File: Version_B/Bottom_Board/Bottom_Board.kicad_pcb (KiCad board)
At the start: 2 copper layers, 74.8 x 84.5 mm, 52 parts, among them J1 Conn_02x03_Top_Bottom, J2 Conn_02x03_Top_Bottom, J3 Conn_01x02_Pin, J5 DIN-5, J6 Conn_01x02_Pin, J7 Conn_01x02_Pin, J8 Screw_Terminal_01x04, J9 Screw_Terminal_01x04, SW2 SW_DIP_x04, U1 LM324, U2 LM324

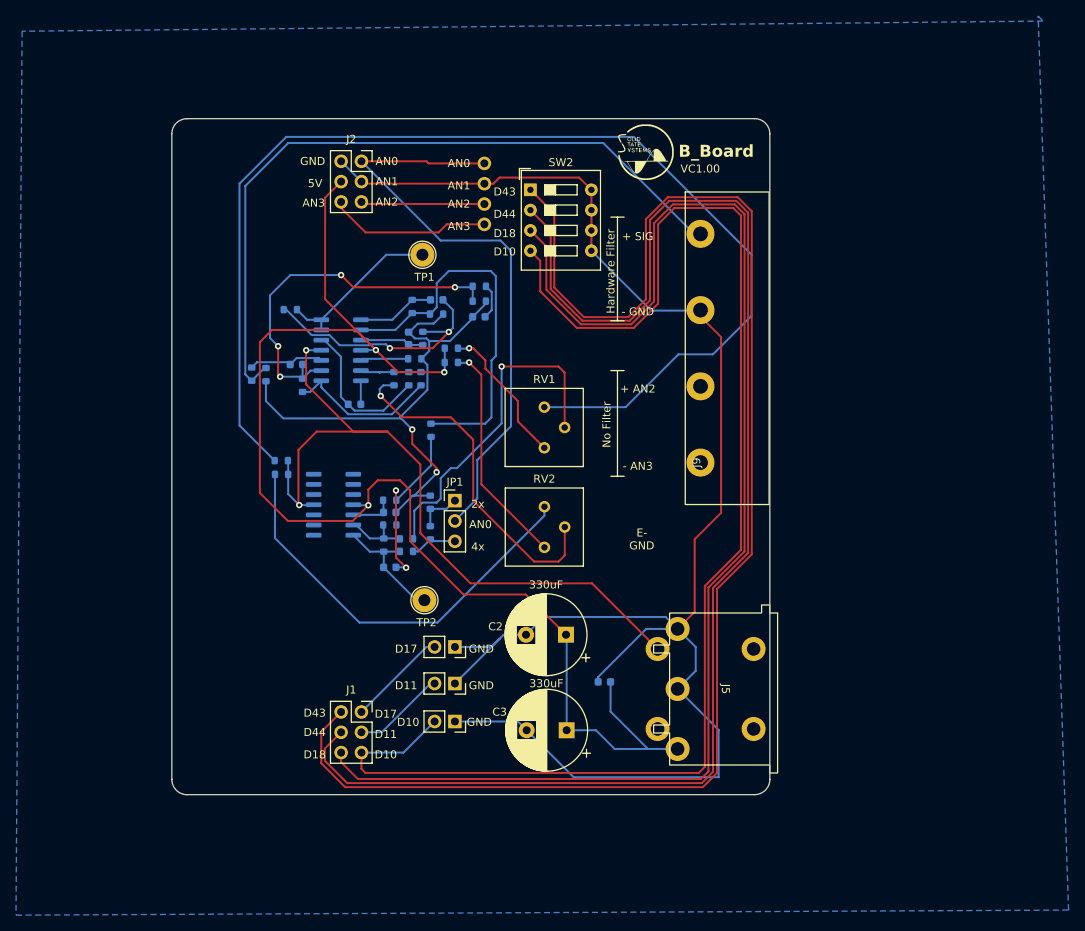
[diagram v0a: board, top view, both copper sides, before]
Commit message: soft pcb changes: 90 degree term block, din connector scooted in, connected grounds
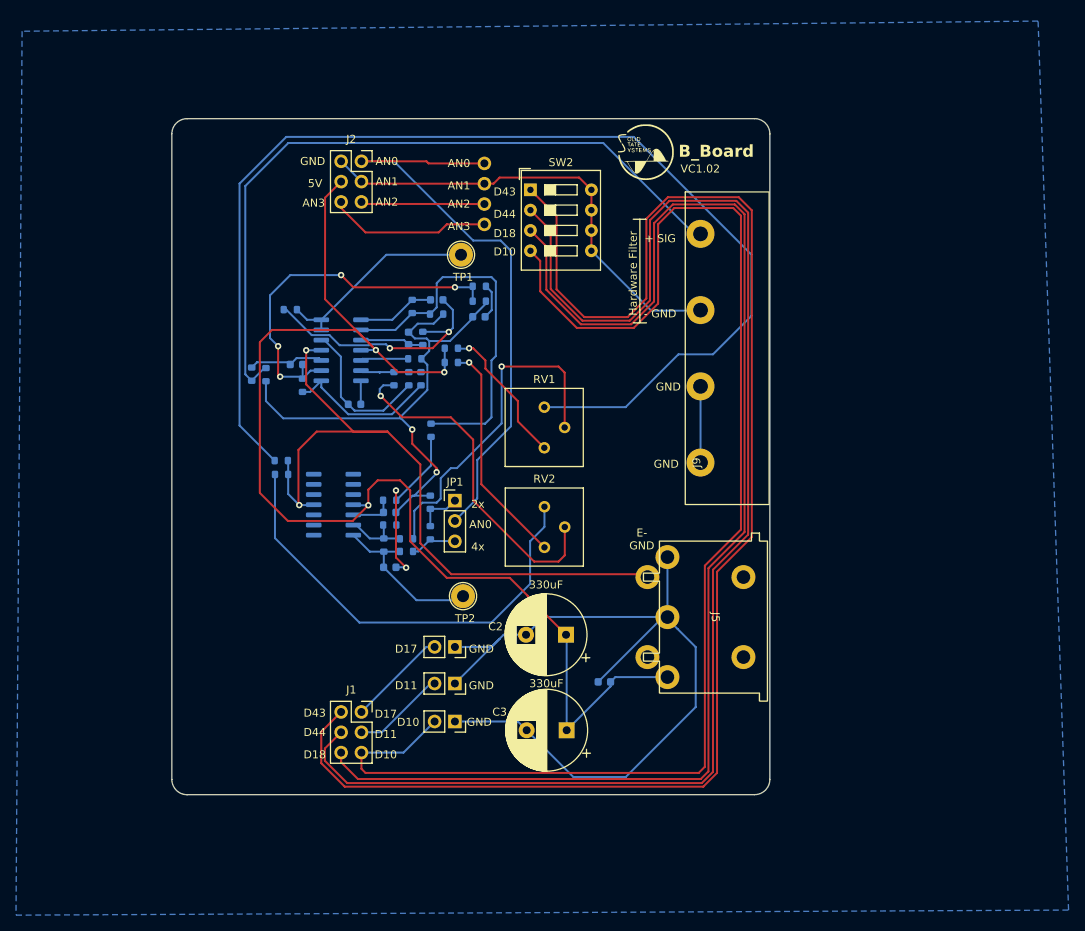
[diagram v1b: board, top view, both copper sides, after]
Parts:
- moved J5 9.07 mm to (167.9, 125.3)
- moved TP2 4.85 mm to (136.4, 122.7)
- moved TP1 4.83 mm to (136.1, 80.0)
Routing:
- net AN1: track 279.0 -> 240.5 mm
- net 5V: track 167.8 -> 158.4 mm
- net Net-(U1D--): track 20.8 -> 25.7 mm
- net Net-(C4-Pad1): track 15.5 -> 20.0 mm
- net -5V: track 95.9 -> 91.6 mm
- net Net-(R18-Pad1): track 52.7 -> 56.6 mm
- net Net-(U1A--): track 47.8 -> 46.8 mm
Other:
- board text added: "VC1.02"
- board text removed: "+ AN2"
- board text removed: "- AN3"
- board text removed: "No Filter"
- board text removed: "VC1.00"

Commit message: ads1015 on bottom board and aesthetic changes
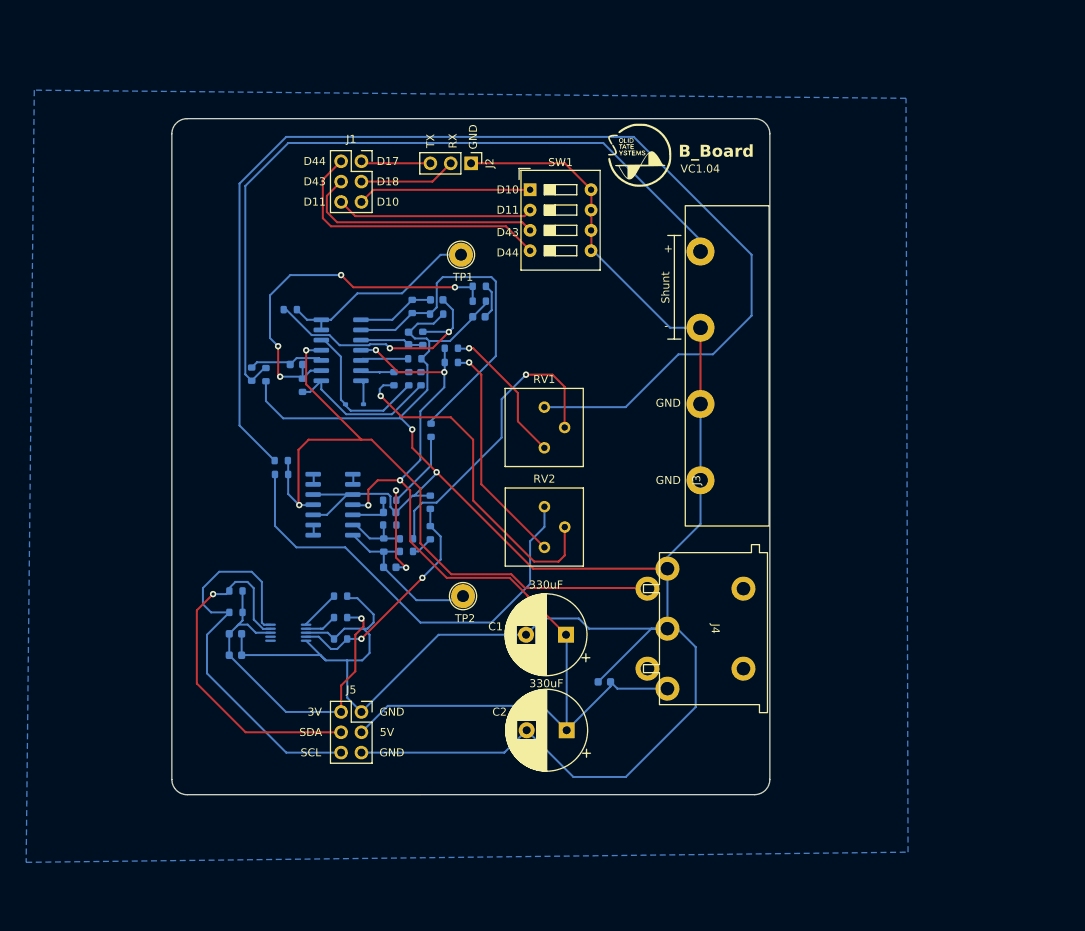
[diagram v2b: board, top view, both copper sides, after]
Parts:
- removed the G*** at (159.3, 67.2)
- removed the J3 at (135.4, 138.4)
- removed J6, J7: Conn_01x02_Pin, Connector_PinSocket_2.54mm:PinSocket_1x02_P2.54mm_Vertical
- removed J8: Screw_Terminal_01x04, Connector_PinHeader_2.54mm:PinHeader_1x04_P2.54mm_Vertical
- removed JP1: Jumper_3_Open, Connector_PinHeader_2.54mm:PinHeader_1x03_P2.54mm_Vertical
- removed SW2: SW_DIP_x04, Button_Switch_THT:SW_DIP_SPSTx04_Slide_9.78x12.34mm_W7.62mm_P2.54mm
- added C10: 0.1uF, Capacitor_SMD:C_0603_1608Metric, B.Cu at (108.0, 130.1)
- added C9: 1uF, Capacitor_SMD:C_0603_1608Metric, B.Cu at (108.0, 127.4)
- added G***: LOGO, bot_lib:logo_SSS, F.Cu at (158.5, 67.6)
- added G***: LOGO, bot_lib:logo_AN, B.Cu at (104.9, 67.1)
- added J2: Conn_01x03_Pin, Connector_PinHeader_2.54mm:PinHeader_1x03_P2.54mm_Vertical, F.Cu at (137.4, 68.6)
- added R26: 10k, Resistor_SMD:R_0603_1608Metric, B.Cu at (121.1, 122.7)
- added R27: 10k, Resistor_SMD:R_0603_1608Metric, B.Cu at (108.0, 122.0)
- added R28: 10k, Resistor_SMD:R_0603_1608Metric, B.Cu at (121.1, 125.4)
- added R29: 10k, Resistor_SMD:R_0603_1608Metric, B.Cu at (108.0, 124.7)
- added R30: 3.9M, Resistor_SMD:R_0603_1608Metric, B.Cu at (121.1, 128.0)
- added SW1: SW_DIP_x04, Button_Switch_THT:SW_DIP_SPSTx04_Slide_9.78x12.34mm_W7.62mm_P2.54mm, F.Cu at (144.8, 71.9)
- added U3: ADS1015IDGSR, bot_lib:DGS0010A_N, B.Cu at (114.6, 127.3)
- D1: value 1N914 -> 1N4148WS; footprint Diode_SMD:D_0603_1608Metric -> bot_lib:Diode_1N4148WS
- J1: renamed from J2; footprint Connector_PinSocket_2.54mm:PinSocket_2x03_P2.54mm_Vertical -> bot_lib:PinSocket_2x03_P2.54mm_Vertical
- J5: renamed from J1; footprint Connector_PinSocket_2.54mm:PinSocket_2x03_P2.54mm_Vertical -> bot_lib:PinSocket_2x03_P2.54mm_Vertical
- RV1, RV2: footprint Potentiometer_THT:Potentiometer_Bourns_3386P_Vertical -> bot_lib:Potentiometer_Bourns_3386P_Vertical
- moved J3 2.21 mm to (166.1, 108.2)
- moved J4 1.44 mm to (167.9, 126.7)
- moved U2 0.06 mm to (120.1, 111.3)
- renumbered C2 to C1, C1 to C11, C3 to C2, C8 to C3, C7 to C4, C9 to C5, C5 to C6, C6 to C7, C4 to C8, J9 to J3, J5 to J4, R10 to R1, R4 to R10, R5 to R11, R16 to R12, R19 to R13, R25 to R14, R11 to R15, R22 to R16, R3 to R17, R14 to R19, R7 to R2, R1 to R20, R13 to R21, R6 to R22, R9 to R23, R12 to R24, R8 to R25, R24 to R3, R23 to R4, R20 to R5, R2 to R6, R21 to R7, R15 to R8, R17 to R9
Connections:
- net 12V renamed +12V
- net 4x_OUTPUT renamed Net-(R21-Pad2)
- C1 pad 1: 5V -> +5VD
- C1 pad 2: AN1 -> GND
- C11 pad 1: 5V -> +5VD
- C11 pad 2: AN1 -> GND
- C2 pad 1: 5V -> +5VD
- C2 pad 2: AN1 -> GND
- C4 pad 2: AN1 -> GND
- C5 pad 2: AN1 -> GND
- C7 pad 1: AN1 -> GND
- J1 pad 1: AN0 -> TX
- J1 pad 2: AN1 -> D44
- J1 pad 3: AN1 -> RX
- J1 pad 4: 5V -> D43
- J1 pad 5: AN2 -> D10
- J1 pad 6: AN3 -> D11
- J3 pad 1: AN1 -> GND
- J3 pad 2: AN1 -> GND
- J3 pad 3: AN1 -> GND
- J4 pad 1: AN1 -> GND
- J4 pad 2: AN1 -> GND
- J4 pad 3: 5V -> +5VD
- J5 pad 1: D17 -> GND
- J5 pad 2: D43 -> +3V0
- J5 pad 3: D11 -> +5VD
- J5 pad 4: D44 -> SDA
- J5 pad 5: D10 -> GND
- J5 pad 6: D18 -> SCL
- R10 pad 2: AN1 -> GND
- R19 pad 1: AN1 -> GND
- R19 pad 2: 2x_OUTPUT -> AN0
- R2 pad 2: AN1 -> GND
- R21 pad 1: 2x_OUTPUT -> AN0
- R23 pad 1: AN1 -> GND
- R3 pad 2: AN1 -> GND
- R6 pad 2: 5V -> +5VD
- R8 pad 1: 5V -> +5VD
- R9 pad 2: AN1 -> GND
- U1 pad 4: 5V -> +5VD
- U2 pad 1: (no net) -> Net-(U2A--)
- U2 pad 10: (no net) -> GND
- U2 pad 12: (no net) -> GND
- U2 pad 13: (no net) -> Net-(U2D--)
- U2 pad 14: (no net) -> Net-(U2D--)
- U2 pad 2: (no net) -> Net-(U2A--)
- U2 pad 3: (no net) -> GND
- U2 pad 4: 5V -> +5VD
- U2 pad 8: (no net) -> Net-(U2C--)
- U2 pad 9: (no net) -> Net-(U2C--)
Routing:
- net GND: track 0.00 -> 366.4 mm, vias 0 -> 2
- net AN1: track 240.5 -> 0.00 mm, vias 2 -> 0
- net D18: track 167.1 -> 0.00 mm
- net 5V: track 158.4 -> 0.00 mm, vias 3 -> 0
- net D43: track 183.3 -> 30.9 mm
- net D10: track 172.0 -> 21.8 mm
- net D44: track 176.3 -> 35.7 mm
- net +5VD: track 0.00 -> 127.2 mm, vias 0 -> 4
- net SCL: track 0.00 -> 50.4 mm
- net AN0: track 75.4 -> 29.0 mm, vias 0 -> 2
- net SDA: track 0.00 -> 45.3 mm, vias 0 -> 1
- net +3V0: track 0.00 -> 45.1 mm, vias 0 -> 1
- net AN3: track 20.4 -> 0.00 mm
- net AN2: track 15.5 -> 0.00 mm
- net D11: track 11.7 -> 24.7 mm
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- added copper zone on B.Cu, net GND
- removed copper zone on B.Cu, net AN1
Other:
- board text added: "+"
- board text added: "-"
- board text added: "3V"
- board text added: "RX"
- board text added: "SCL"
- board text added: "SDA"
- board text added: "Shunt"
- board text added: "TX"
- board text added: "VC1.04"
- board text removed: "+ SIG"
- board text removed: "- GND"
- board text removed: "2x"
- board text removed: "4x"
- board text removed: "AN0"
- board text removed: "AN1"
- board text removed: "AN2"
- board text removed: "AN3"
- board text removed: "E- GND"
- board text removed: "Hardware Filter"
- board text removed: "VC1.02"
